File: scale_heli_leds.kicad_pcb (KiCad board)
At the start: 2 copper layers, 28.2 x 16 mm, 22 parts, among them IC1 ATTINY85-S, J1 CONN_XH_4POS, J2 HEADER_4POS_2.50mm, P1 pkl_USB_OTG, U1 USBLC6-2, U2 CL320SG-G, U3 MIC5225-3.3V

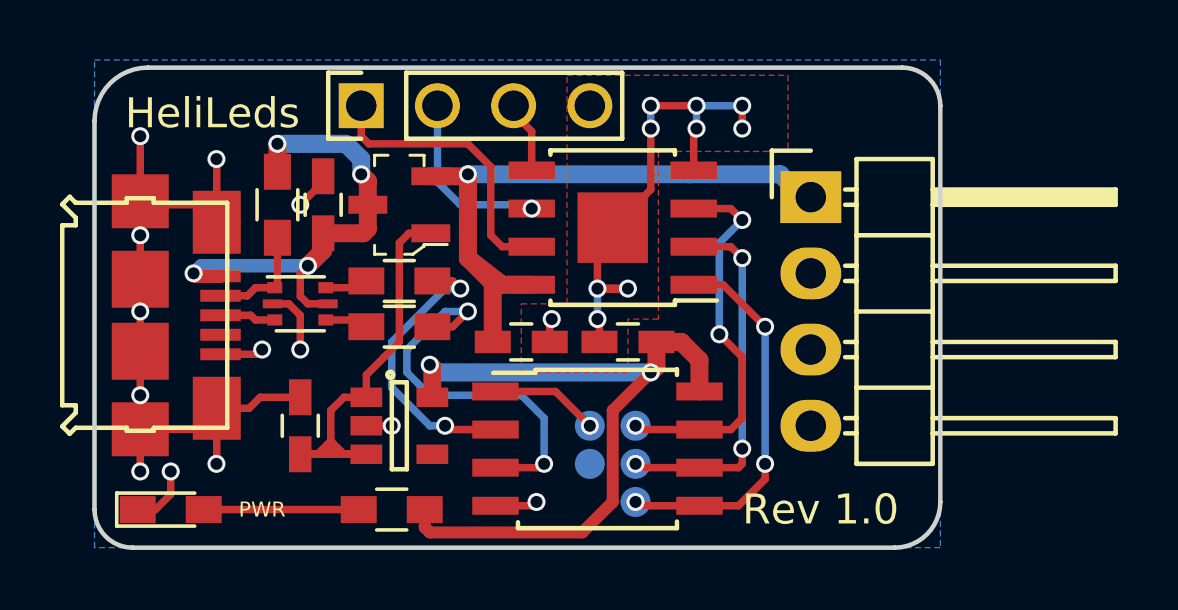
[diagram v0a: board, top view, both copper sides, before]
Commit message: Updated to Rev1.1: Fixed battery connector orientation, fixed incorrect BAT54C schematic symbol pin numbers, removed programming pads.
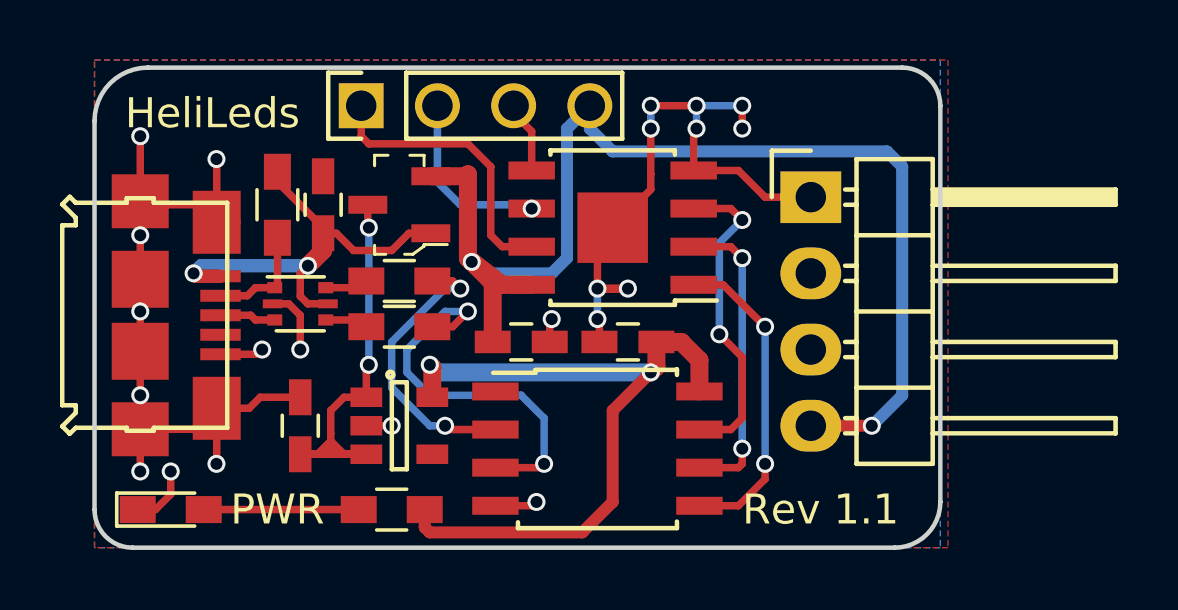
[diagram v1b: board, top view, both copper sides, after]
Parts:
- removed GND1, MISO1, MOSI1, SCK1: POGO_PAD_SMD, pkl_pads:PAD_SMD_R_1x1
- removed RESET1: RESET, pkl_pads:PAD_SMD_R_1x1
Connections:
- D1 pad 1: Net-(C1-Pad1) -> +5V
- D1 pad 3: +5V -> Net-(C1-Pad1)
- IC1 pad 1: /RESET -> (no net)
- J1 pad 1: +BATT -> GND
- J1 pad 2: Net-(J1-Pad2) -> (no net)
- J1 pad 3: Net-(J1-Pad3) -> (no net)
- J1 pad 4: GND -> +BATT
- J2 pad 4: GND -> +BATT
- P1 pad 4: Net-(P1-Pad4) -> (no net)
- U3 pad 4: Net-(U3-Pad4) -> (no net)
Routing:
- net +BATT: track 21.4 -> 41.4 mm, vias 1 -> 2
- net /RESET: track 3.62 -> 0.00 mm, vias 1 -> 0
- net GND: track 56.8 -> 60.0 mm, vias 23 -> 22
- net /MOSI: track 12.8 -> 10.6 mm, vias 3 -> 2
- net /SCK: track 12.8 -> 10.6 mm, vias 3 -> 2
- net /MISO: track 12.3 -> 10.1 mm, vias 3 -> 2
- net +5V: track 16.2 -> 15.0 mm, vias 4 -> 2
- net Net-(C1-Pad1): track 16.3 -> 16.0 mm, vias 0 -> 2
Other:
- rule pad_to_mask_clearance: 0.2 -> 0.0508
- rule trace_min: 0.2 -> 0
- rule via_min_drill: 0.3 -> 0.254
- rule via_min_size: 0.4 -> 0.508
- board text added: "Rev 1.1"
- board text added: "VBATT+"
- board text removed: "GND"
- board text removed: "Rev 1.0"
